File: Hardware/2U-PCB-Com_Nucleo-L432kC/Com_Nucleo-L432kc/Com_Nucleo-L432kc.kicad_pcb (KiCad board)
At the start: 2 copper layers, 90 x 92 mm, 44 parts, among them IC1 PCI_EXPRESS_CARD, J1 Bus Standard, J10 Conn_01x01, J2 I2C_Grove, J3 I2C_Grove, J4 Conn_01x08, J5 Conn_01x08, J6 Conn_01x15, J7 Conn_01x15, J8 I2C_Grove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

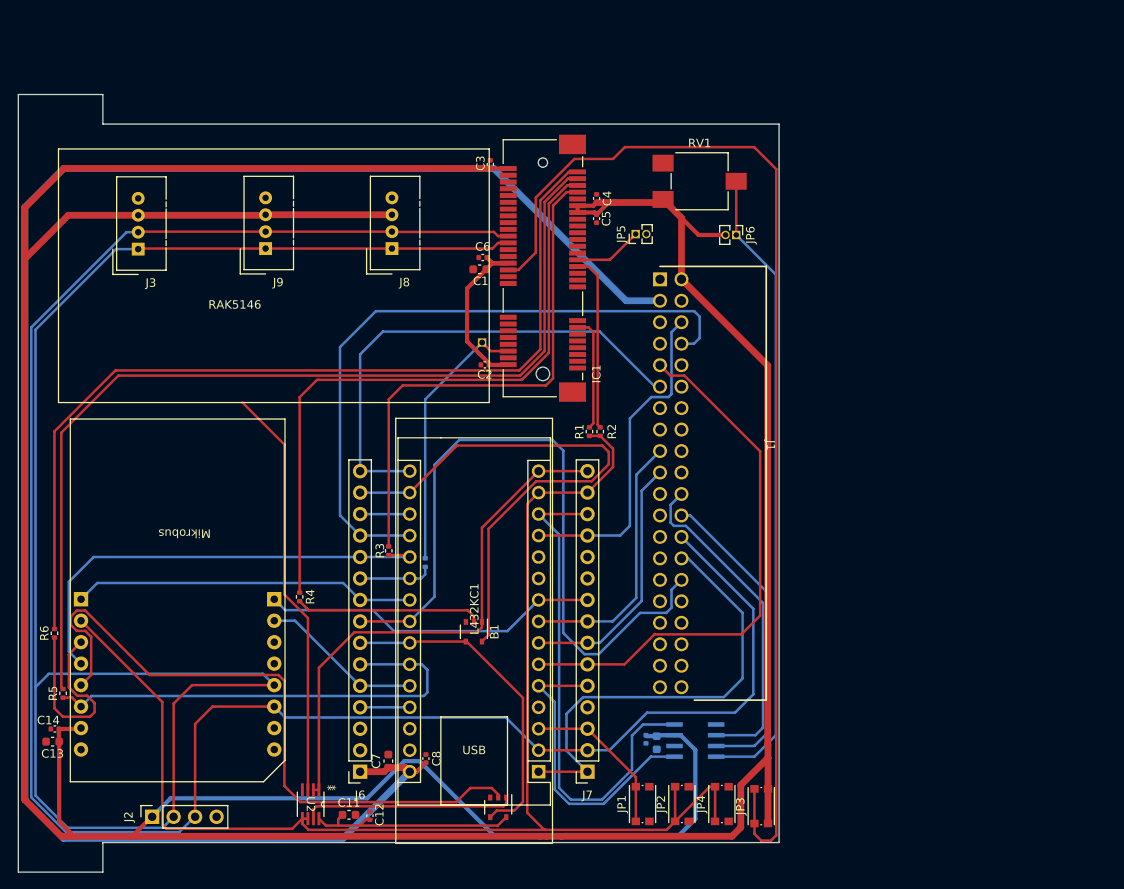
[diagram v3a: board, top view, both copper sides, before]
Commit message: New library joined, cause we changed for a 7404 logic gate. All the routes were re-made.
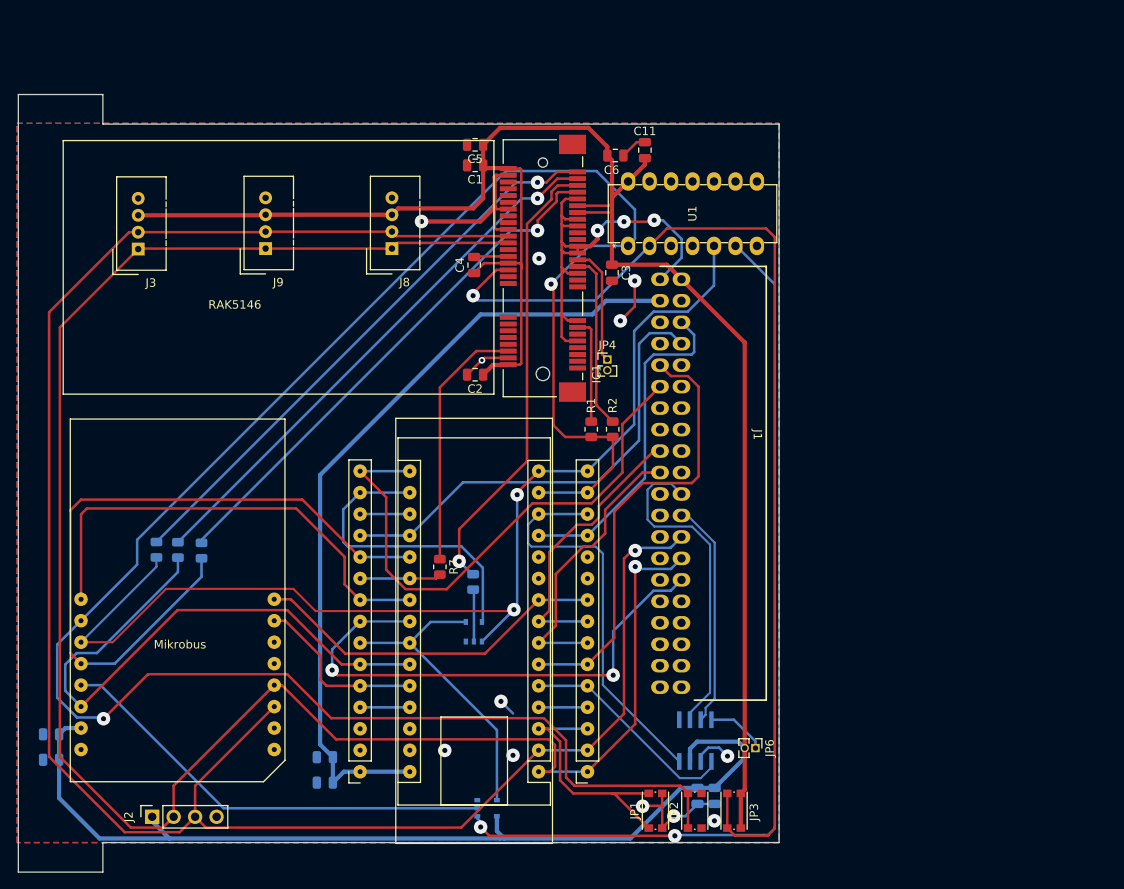
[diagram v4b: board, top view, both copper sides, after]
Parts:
- removed C12: 100n, Capacitor_SMD:C_0402_1005Metric
- removed J10: Conn_01x01, Connector_PinSocket_1.27mm:PinSocket_1x01_P1.27mm_Vertical
- removed the JP4 at (147.0, 127.0)
- removed RV1: R_Potentiometer_Trim, Potentiometer_SMD:Potentiometer_ACP_CA6-VSMD_Vertical
- removed U2: 74LVC2G02, SN74LVC2G02_SSOP:DCT8
- added U1: 7404, ul_SN74HC04N:N14, F.Cu at (135.9, 61.0)
- B1, B2: moved to B.Cu
- C1, C9: footprint Capacitor_SMD:C_0603_1608Metric -> Capacitor_SMD:C_0805_2012Metric
- C10, C2, C3, C4, C5, C6: footprint Capacitor_SMD:C_0402_1005Metric -> Capacitor_SMD:C_0805_2012Metric
- C11: value 10u -> 100n; footprint Capacitor_SMD:C_0603_1608Metric -> Capacitor_SMD:C_0805_2012Metric
- C13, C7: footprint Capacitor_SMD:C_0603_1608Metric -> Capacitor_SMD:C_0805_2012Metric; moved to B.Cu
- C14, C8: footprint Capacitor_SMD:C_0402_1005Metric -> Capacitor_SMD:C_0805_2012Metric; moved to B.Cu
- L432KC1: value ~ -> MCU
- R1, R2: footprint Resistor_SMD:R_0402_1005Metric -> Resistor_SMD:R_0805_2012Metric
- R3, R4, R5, R6: footprint Resistor_SMD:R_0402_1005Metric -> Resistor_SMD:R_0805_2012Metric; moved to B.Cu
- R7: footprint Resistor_SMD:R_0402_1005Metric -> Resistor_SMD:R_0805_2012Metric; moved to F.Cu
- moved C11 86.1 mm to (137.9, 49.6), turned to 90 degrees
- moved JP6 60.7 mm to (151.0, 120.4)
- moved R3 22.1 mm to (85.4, 97.0)
- moved R5 21.7 mm to (82.6, 96.9)
- moved R4 20.6 mm to (117.6, 100.7)
- moved C6 19.8 mm to (134.4, 50.3), turned to 0 degrees
- moved C3 19.3 mm to (134.0, 64.1), turned to -90 degrees
- moved C5 16.8 mm to (117.8, 49.0), turned to 180 degrees
- moved C4 16.5 mm to (117.7, 63.2)
- moved R6 15.6 mm to (80.1, 96.9)
- moved JP4 15.2 mm to (133.4, 74.4), turned to 0 degrees
- moved C1 12.3 mm to (117.8, 51.4)
- moved C8 12.3 mm to (100.0, 124.5), turned to 180 degrees
- moved C9 9.31 mm to (146.1, 126.0)
- moved C10 9.06 mm to (144.1, 126.0)
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- renumbered JP5 to JP4
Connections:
- B1 pad 5: +3V3 -> /3.3V
- J6 pad 14: +3V3 -> /3.3V
- L432KC1 pad 17: +3V3 -> /3.3V
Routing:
- net +3V3: track 590.7 -> 323.3 mm
- net GND: track 0.00 -> 119.5 mm, vias 0 -> 15
- net /Vin: track 213.6 -> 95.4 mm
- net Net-(B2-OE): track 24.9 -> 107.9 mm, vias 0 -> 2
- net /MCU_NRESET: track 163.1 -> 245.4 mm, vias 0 -> 2
- net Net-(CR1-ASC): track 75.6 -> 7.06 mm
- net /SX1303_RESET: track 179.0 -> 125.1 mm, vias 0 -> 1
- net Net-(IC1-RESERVED3): track 114.3 -> 65.1 mm, vias 0 -> 1
- net /CS_MCU: track 88.0 -> 132.7 mm, vias 0 -> 2
- net Net-(IC1-RESERVED4): track 108.3 -> 68.0 mm, vias 0 -> 1
- net /3.3V: track 0.00 -> 36.8 mm
- net /HOST_SCK: track 54.4 -> 83.2 mm
- net /MKB_MISO: track 79.1 -> 52.9 mm
- net /SENS_ROUE/MAG-X: track 78.7 -> 55.4 mm
- net Net-(IC1-RESERVED2): track 76.7 -> 53.9 mm, vias 0 -> 1
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- added copper zone on B.Cu, net GND
- added copper zone on F.Cu, net GND

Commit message: The board is ready, need some revision
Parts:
- removed JP6: speed_controller, Connector_PinHeader_1.27mm:PinHeader_1x02_P1.27mm_Vertical
- added JP5: speed_controller, Connector_PinHeader_2.54mm:PinHeader_1x02_P2.54mm_Vertical, F.Cu at (152.2, 121.3)
- JP4: footprint Connector_PinHeader_1.27mm:PinHeader_1x02_P1.27mm_Vertical -> Connector_PinHeader_2.54mm:PinHeader_1x02_P2.54mm_Vertical
- moved JP4 0.19 mm to (133.6, 74.3)
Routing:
- net GND: track 119.5 -> 145.9 mm, vias 15 -> 21
- net /SENS_ROUE/MAG-X: track 55.4 -> 59.6 mm
- net Net-(CR1-ASC): track 7.06 -> 8.47 mm
- net +3V3: track 323.3 -> 324.2 mm
- net /CAN1_TX: track 26.9 -> 26.2 mm
- net Net-(B2-OE): track 107.9 -> 108.6 mm
- net /RX_CALC: track 34.0 -> 33.4 mm
- net /SENS_MAG-Y: track 65.9 -> 65.4 mm
- net /CAN_RD: track 38.7 -> 39.2 mm
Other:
- board text added: "3V3"
- board text added: "GND"
- board text added: "SCL"
- board text added: "SDA"

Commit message: First version for fabrication
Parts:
- added REF**: MountingHole_3.5mm, MountingHole:MountingHole_3.5mm, F.Cu at (72.9, 52.3)
- added REF**: MountingHole_3.5mm, MountingHole:MountingHole_3.5mm, F.Cu at (73.1, 77.5)
- moved J7 1.46 mm to (129.6, 123.2)
- moved J6 1.31 mm to (105.5, 123.2)
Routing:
- net GND: track 145.9 -> 129.2 mm, vias 21 -> 22
- net /AN: track 55.6 -> 43.5 mm, vias 0 -> 1
- net /CS_MCU: track 132.7 -> 126.3 mm, vias 2 -> 3
- net /SCL: track 225.4 -> 219.2 mm, vias 1 -> 4
- net /MCU_NRESET: track 245.4 -> 250.1 mm
- net /MCU_MOSI: track 71.6 -> 76.1 mm, vias 0 -> 1
- net /HOST_SCK: track 82.8 -> 78.4 mm, vias 0 -> 1
- net /SENS_ROUE/MAG-X: track 59.6 -> 55.4 mm
- net +3V3: track 324.2 -> 320.1 mm
- net /3.3V: track 36.8 -> 39.0 mm
- net /SX1303_RESET: track 125.3 -> 123.3 mm
- net /TX_CALC: track 33.8 -> 32.1 mm
- net /RX_CALC: track 33.4 -> 32.0 mm
- net /MISO: track 36.4 -> 35.1 mm
- net /GPIO(6): track 9.62 -> 8.32 mm
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
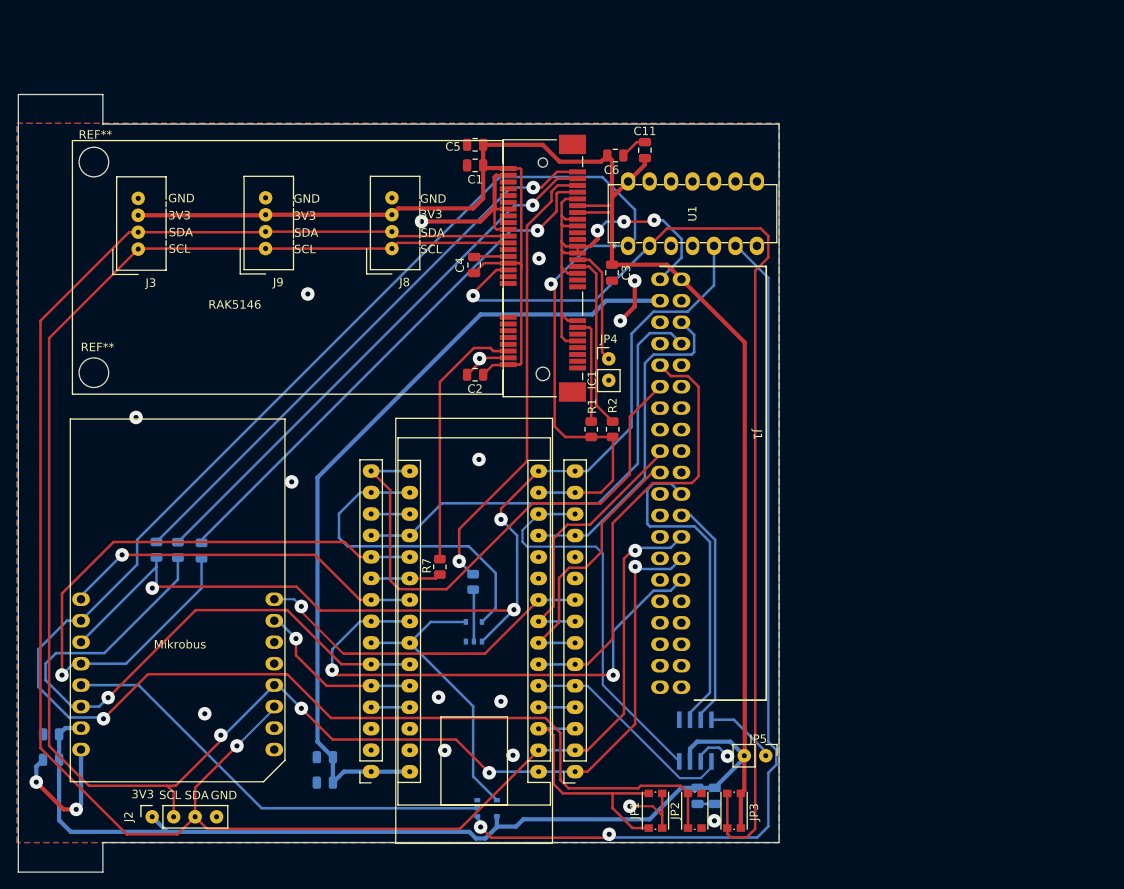
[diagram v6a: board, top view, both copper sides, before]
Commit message: Flatsat connector was in the wrong side. All the routes were remade.
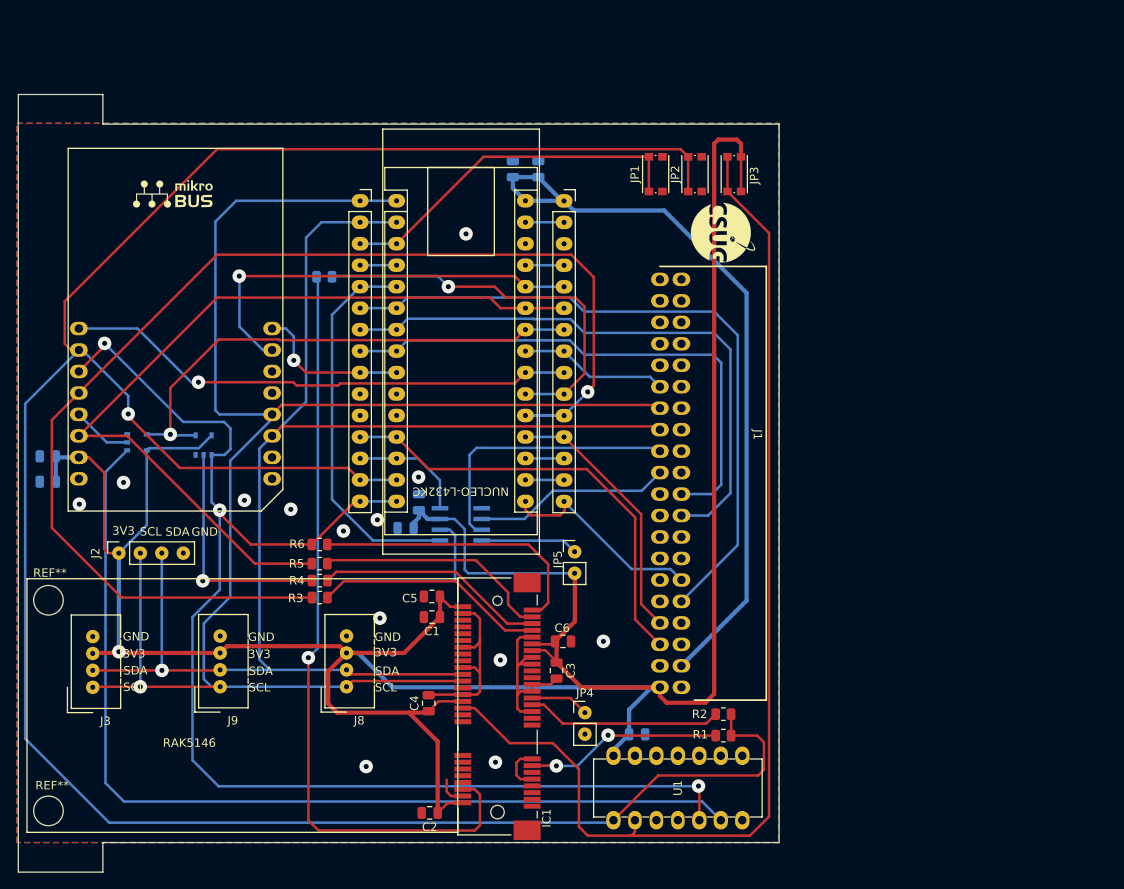
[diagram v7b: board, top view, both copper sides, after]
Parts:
- added G***: LOGO, Logos-image:mikrobus_logo, F.Cu at (81.8, 54.7)
- added G***: LOGO, Logos-image:Image-Csug_10x10, F.Cu at (147.1, 59.4)
- C11, R7: moved to B.Cu
- R3, R4, R5, R6: moved to F.Cu
- moved C8 75.9 mm to (122.3, 51.9), turned to 90 degrees
- moved JP1 75.3 mm to (139.1, 52.5)
- moved JP2 75.3 mm to (143.8, 52.5)
- moved JP3 75.3 mm to (148.4, 52.5)
- moved C7 74.0 mm to (125.3, 51.9), turned to 90 degrees
- moved J7 72.2 mm to (104.2, 55.6), turned to 0 degrees
- moved J6 71.3 mm to (128.3, 55.6), turned to 0 degrees
- moved L432KC1 69.6 mm to (108.5, 55.6), turned to 0 degrees
- moved C11 69.1 mm to (137.0, 118.7), turned to 0 degrees
- moved U1 68.0 mm to (134.2, 128.9)
- moved B2 59.9 mm to (77.8, 84.2)
- moved C6 57.8 mm to (128.2, 107.7)
- moved C1 53.7 mm to (112.7, 104.9)
- moved C5 53.7 mm to (112.7, 102.4)
- moved J3 52.1 mm to (72.6, 113.2)
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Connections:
- B1 pad 5: /3.3V -> +3V3
- J7 pad 7: /TX_CALC -> /RX_CALC
- J7 pad 8: /RX_CALC -> /TX_CALC
- L432KC1 pad 7: /TX_CALC -> /RX_CALC
- L432KC1 pad 8: /RX_CALC -> /TX_CALC
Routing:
- net /HOST_SCK: track 78.4 -> 147.2 mm
- net /SDA: track 233.9 -> 169.8 mm, vias 2 -> 1
- net /TH1: track 30.9 -> 91.8 mm, vias 0 -> 1
- net GND: track 129.2 -> 69.3 mm, vias 22 -> 13
- net /MKB_MISO: track 52.9 -> 7.08 mm
- net /RESET_SIGNAL: track 62.3 -> 17.7 mm, vias 2 -> 0
- net /MCU_NRESET: track 250.1 -> 290.8 mm, vias 2 -> 1
- net /SENS_MAG-Y: track 64.6 -> 25.0 mm
- net /GPIO(6): track 8.32 -> 47.3 mm, vias 0 -> 1
- net /RX_CALC: track 32.0 -> 69.8 mm
- net Net-(IC1-RESERVED3): track 65.2 -> 28.0 mm, vias 1 -> 0
- net Net-(IC1-RESERVED1): track 63.1 -> 27.4 mm, vias 1 -> 0
- net /3.3V: track 39.0 -> 4.57 mm
- net Net-(IC1-RESERVED4): track 68.0 -> 34.8 mm, vias 1 -> 0
- net /CAN1_RX: track 46.8 -> 13.8 mm
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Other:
- board text added: "NUCLEO-L432KC"
- board text removed: "Mikrobus"

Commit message: push leo
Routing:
- net Net-(IC1-REFCLK+): track 23.3 -> 23.2 mm, vias 2 -> 0
